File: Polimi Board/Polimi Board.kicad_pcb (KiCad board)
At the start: 2 copper layers, 96 parts, among them IC1 M95512-RMN6P, J1 I2C Oled Screen, J2 DM3AT-SF-PEJM5_40_, J3 65100516121, J4 UART Conn, J5 JTAG Conn, J7 65100516121, J8 7499010121A, SW1 MCU Reset, SW2 SW_Push, SW3 SW_Push, SW4 SW_Push, SW5 SW_Push, SW6 SW_Push, SW7 SW_Push, SW8 SW_Push, U1 STM32F205RCT6, U2 FT2232HL, U3 LAN8742A, U5 TLV76133DCY, Y1 ABL-25.000MHz-B1UB, Y2 ABL-12.000MHZ-20-D4HFI

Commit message: PCB wip
before holidays
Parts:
- removed R33, R34, R35, R36, R37, R38, R39: 47k, Resistor_SMD:R_0603_1608Metric_Pad0.98x0.95mm_HandSolder
- removed U5: TLV76133DCY, Package_TO_SOT_SMD:SOT-223-3_TabPin2
- added J6: DM3AT-SF-PEJM5_40_, SamacSys_Parts:DM3ATSFPEJM540, F.Cu at (185.7, 106.4)
- added J9: Conn_01x07_Pin, Connector_PinHeader_2.54mm:PinHeader_1x07_P2.54mm_Vertical, F.Cu at (197.8, 82.5)
- added R10: 47k, Resistor_SMD:R_0603_1608Metric_Pad0.98x0.95mm_HandSolder, F.Cu at (178.6, 107.9)
- added R11: 47k, Resistor_SMD:R_0603_1608Metric_Pad0.98x0.95mm_HandSolder, F.Cu at (181.3, 107.8)
- added R12: 47k, Resistor_SMD:R_0603_1608Metric_Pad0.98x0.95mm_HandSolder, F.Cu at (181.3, 111.5)
- added R14: 47k, Resistor_SMD:R_0603_1608Metric_Pad0.98x0.95mm_HandSolder, F.Cu at (178.6, 111.5)
- added R15: 47k, Resistor_SMD:R_0603_1608Metric_Pad0.98x0.95mm_HandSolder, F.Cu at (176.1, 111.5)
- added R9: 47k, Resistor_SMD:R_0603_1608Metric_Pad0.98x0.95mm_HandSolder, F.Cu at (176.1, 107.9)
- added REF**: MountingHole_3.2mm_M3_DIN965_Pad, MountingHole:MountingHole_3.2mm_M3_DIN965_Pad, F.Cu at (106.0, 45.0)
- added REF**: MountingHole_3.2mm_M3_DIN965_Pad, MountingHole:MountingHole_3.2mm_M3_DIN965_Pad, F.Cu at (198.0, 45.0)
- added REF**: MountingHole_3.2mm_M3_DIN965_Pad, MountingHole:MountingHole_3.2mm_M3_DIN965_Pad, F.Cu at (198.0, 137.0)
- added REF**: MountingHole_3.2mm_M3_DIN965_Pad, MountingHole:MountingHole_3.2mm_M3_DIN965_Pad, F.Cu at (106.0, 137.0)
- added U4: TLV76133DCY, Package_TO_SOT_SMD:SOT-223-3_TabPin2, F.Cu at (163.1, 56.6)
- J2: value DM3AT-SF-PEJM5_40_ -> 65100516121; footprint SamacSys_Parts:DM3ATSFPEJM540 -> SamacSys_Parts:65100516121
- J7: value 65100516121 -> 7499010121A; footprint SamacSys_Parts:65100516121 -> SamacSys_Parts:WURTH-7499010121A
- J8: value 7499010121A -> Conn_01x07_Pin; footprint SamacSys_Parts:WURTH-7499010121A -> Connector_PinHeader_2.54mm:PinHeader_1x07_P2.54mm_Vertical
- SW2: value SW_Push -> Boot
- moved R30 84.0 mm to (183.5, 130.2), turned to 180 degrees
- moved D1 83.4 mm to (172.2, 47.8), turned to 180 degrees
- moved R27 79.9 mm to (151.3, 134.1), turned to -90 degrees
- moved R29 79.5 mm to (172.0, 130.2), turned to 180 degrees
- moved R2 77.1 mm to (114.4, 62.9), turned to -90 degrees
- moved SW3 72.2 mm to (115.5, 122.0)
- moved R26 71.9 mm to (128.3, 126.0)
- moved R1 71.2 mm to (171.2, 53.5), turned to 90 degrees
- moved D4 71.0 mm to (157.2, 134.2), turned to 180 degrees
- moved R24 70.5 mm to (118.8, 118.5)
- moved JP4 66.6 mm to (109.5, 111.1), turned to -90 degrees
- moved SW8 66.4 mm to (180.4, 121.9)
- moved SW5 62.6 mm to (125.0, 129.4)
- moved SW7 61.0 mm to (168.7, 121.9)
- moved C23 59.4 mm to (116.3, 82.9), turned to 90 degrees
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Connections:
- J2 pad 1: /SDMMC_D2 -> /USB Programming and OTP/VBUS_PROG
- J2 pad 2: /SDMMC_D3 -> Net-(U2-DM)
- J2 pad 3: /SDMMC_CMD -> Net-(U2-DP)
- J2 pad 4: +3.3V -> unconnected-(J2-Pad4)
- J2 pad 5: /SDMMC_CK -> GND
- J3 pad 1: /USB Programming and OTP/VBUS_PROG -> /USB Programming and OTP/VBUS_OTG
- J3 pad 2: Net-(U2-DM) -> /OTG_DM
- J3 pad 3: Net-(U2-DP) -> /OTG_DP
- J7 pad 1: /USB Programming and OTP/VBUS_OTG -> /Ethernet/TXP
- J7 pad 2: /OTG_DM -> +3V3
- J7 pad 3: /OTG_DP -> /Ethernet/TXN
- J7 pad 4: unconnected-(J7-Pad4) -> /Ethernet/RXP
- J7 pad 5: GND -> +3V3
- J8 pad 1: /Ethernet/TXP -> +3.3V
- J8 pad 2: +3V3 -> /GPIO_EXT_1
- J8 pad 3: /Ethernet/TXN -> /GPIO_EXT_2
- J8 pad 4: /Ethernet/RXP -> /GPIO_EXT_3
- J8 pad 5: +3V3 -> /GPIO_EXT_4
- J8 pad 6: /Ethernet/RXN -> /GPIO_EXT_5
- J8 pad 7: unconnected-(J8-Pad7) -> GND
- R16 pad 1: Net-(J8-Pad11) -> Net-(J7-Pad10)
- R16 pad 2: GND -> /Ethernet/LED1
- R17 pad 1: Net-(J8-Pad9) -> /Ethernet/LED2
- R17 pad 2: GND -> Net-(J7-Pad12)
- U1 pad 14: unconnected-(U1-PA0-Pad14) -> /GPIO_EXT_1
- U1 pad 16: unconnected-(U1-PA2-Pad16) -> /GPIO_EXT_2
- U1 pad 17: unconnected-(U1-PA3-Pad17) -> /GPIO_EXT_3
- U1 pad 26: unconnected-(U1-PB0-Pad26) -> /GPIO_EXT_4
- U1 pad 27: unconnected-(U1-PB1-Pad27) -> /GPIO_EXT_5
- U1 pad 28: unconnected-(U1-PB2-Pad28) -> /GPIO_EXT_6
- U1 pad 29: unconnected-(U1-PB10-Pad29) -> /GPIO_EXT_9
- U1 pad 38: /SDMMC_WP -> /GPIO_EXT_10
- U1 pad 61: unconnected-(U1-PB8-Pad61) -> /GPIO_EXT_7
- U1 pad 62: unconnected-(U1-PB9-Pad62) -> /GPIO_EXT_8
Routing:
- net GND: track 0.00 -> 171.4 mm
- net +3.3V: track 0.00 -> 103.0 mm
- net /USB Programming and OTP/JTAG_SRST: track 0.00 -> 54.1 mm
- net /Ethernet/RXN: track 0.00 -> 52.4 mm
- net /JTAG_TD0: track 0.00 -> 46.1 mm
- net /SDMMC_CMD: track 0.00 -> 45.6 mm
- net Net-(U2-DP): track 0.00 -> 45.0 mm, vias 0 -> 2
- net Net-(U2-DM): track 0.00 -> 44.7 mm, vias 0 -> 2
- net /JTAG_TRST: track 0.00 -> 36.5 mm
- net /Ethernet/TXP: track 0.00 -> 34.0 mm
- net /JTAG_TMS: track 0.00 -> 33.5 mm
- net /JTAG_TDI: track 0.00 -> 31.6 mm
- net /Flash_MOSI: track 0.00 -> 31.4 mm, vias 0 -> 2
- net /Ethernet/RXP: track 0.00 -> 30.6 mm
- net Net-(U2-ACBUS4): track 0.00 -> 29.9 mm
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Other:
- board outline added: 100 x 100 mm

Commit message: almost finish
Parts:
- added G***: LOGO, graphics:Logo, B.Cu at (141.0, 98.6)
- J4: value UART Conn -> UART
- JP4: value MCU_RST -> MCU RST
- moved SW1 82.0 mm to (107.5, 133.1), turned to 180 degrees
- moved J6 81.3 mm to (105.8, 121.3), turned to -90 degrees
- moved SW2 79.6 mm to (170.6, 107.2)
- moved R11 72.3 mm to (110.2, 120.7), turned to -90 degrees
- moved R12 71.4 mm to (110.2, 117.1), turned to 90 degrees
- moved R2 70.6 mm to (161.9, 115.1)
- moved R10 66.9 mm to (112.9, 120.6), turned to -90 degrees
- moved R14 65.9 mm to (112.9, 117.1), turned to 90 degrees
- moved R9 62.0 mm to (115.4, 120.6), turned to -90 degrees
- moved R15 60.9 mm to (115.4, 117.1), turned to 90 degrees
- moved J2 44.8 mm to (109.2, 70.4)
- moved JP2 43.3 mm to (142.0, 70.0), turned to 0 degrees
- moved C8 39.4 mm to (132.0, 103.0), turned to 180 degrees
- moved C5 38.8 mm to (132.0, 101.0), turned to 180 degrees
- moved JP1 38.0 mm to (136.0, 70.0), turned to 0 degrees
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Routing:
- net GND: track 171.4 -> 675.1 mm, vias 0 -> 14
- net +3.3V: track 103.0 -> 521.0 mm, vias 0 -> 16
- net /USART_TX: track 0.00 -> 156.6 mm, vias 0 -> 2
- net /USART_RX: track 0.00 -> 153.5 mm, vias 0 -> 2
- net /MCU_RST: track 17.8 -> 122.3 mm, vias 0 -> 3
- net /GPIO_EXT_10: track 0.00 -> 71.7 mm, vias 0 -> 1
- net /MCO: track 6.96 -> 77.3 mm, vias 0 -> 2
- net /GPIO_EXT_9: track 0.00 -> 69.2 mm, vias 0 -> 1
- net /GPIO_EXT_5: track 0.00 -> 67.4 mm, vias 0 -> 1
- net /GPIO1: track 0.00 -> 62.7 mm, vias 0 -> 1
- net /GPIO_EXT_4: track 0.00 -> 61.7 mm, vias 0 -> 2
- net /GPIO_EXT_7: track 0.00 -> 59.6 mm, vias 0 -> 2
- net /GPIO_EXT_6: track 0.00 -> 59.1 mm, vias 0 -> 1
- net +3V3: track 27.0 -> 85.7 mm, vias 0 -> 2
- net Net-(U1-BOOT0): track 9.45 -> 67.1 mm, vias 0 -> 1
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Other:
- board size 100 x 100 mm -> 100 x 70 mm
- board text added: "FS"
- board text added: "HS"
- board text added: "OTG DM"
- board text added: "OTG DP"

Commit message: Final version
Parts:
- D2: value TXLED -> tx
- D3: value RXLED -> rx
- moved G*** 1.69 mm to (140.0, 100.0)
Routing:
- net Net-(U2-DP): track 28.8 -> 31.5 mm
- net Net-(U2-DM): track 25.5 -> 27.5 mm
- net /ETH_RMII_TXD0: track 60.1 -> 59.2 mm
- net /ETH_RMII_TX_EN: track 51.8 -> 52.3 mm
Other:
- board text added: "STM32F205RCT6 Board V1.0"

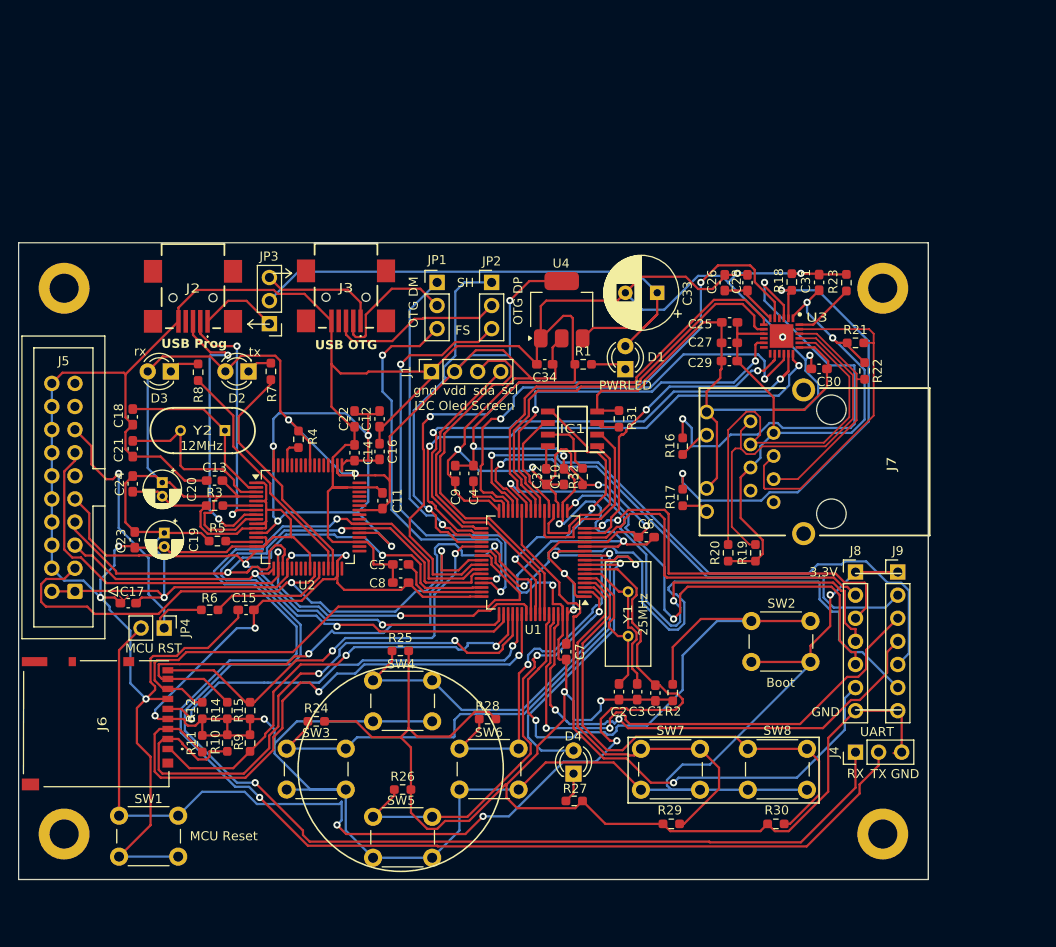
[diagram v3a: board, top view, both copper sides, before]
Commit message: Set zero at top left corner of PCB
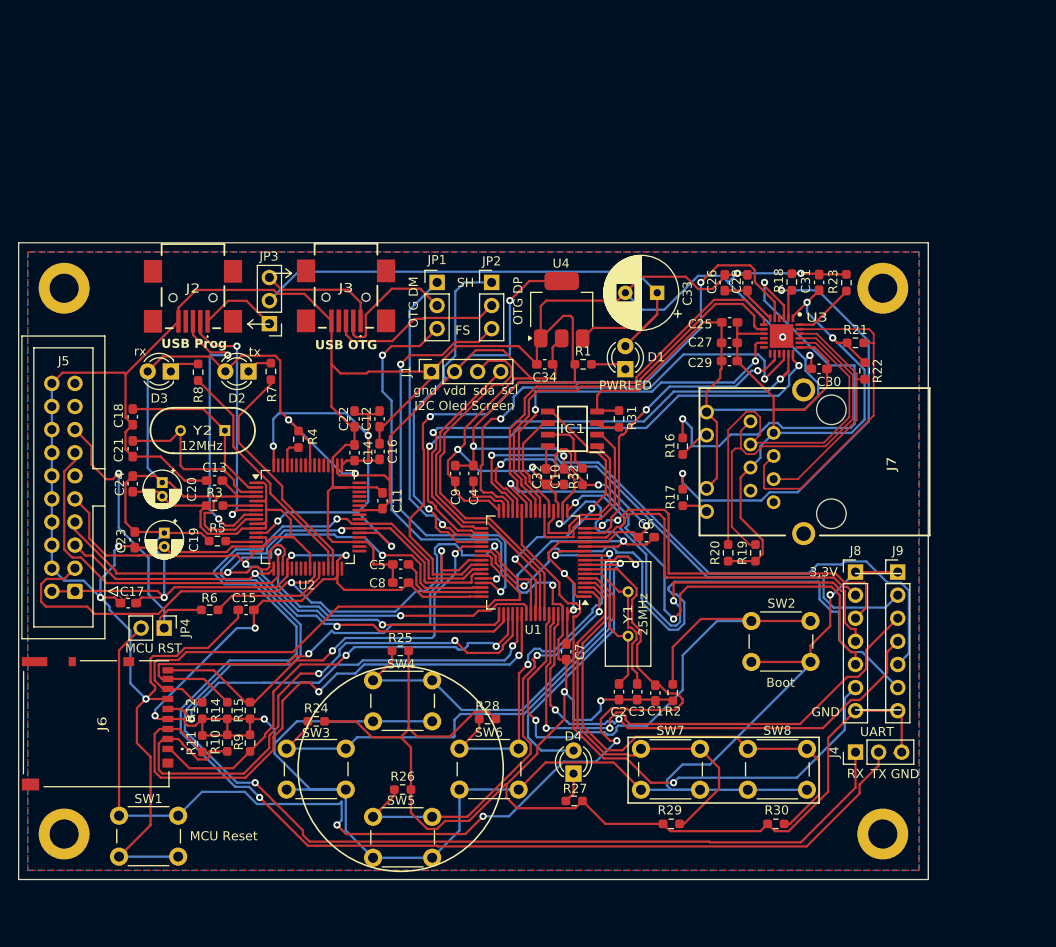
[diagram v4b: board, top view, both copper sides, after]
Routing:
- net +1V8: track 68.6 -> 60.1 mm
- added copper zone on B.Cu, net GND
- added copper zone on F.Cu, net GND
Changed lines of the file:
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@@
 		(pad_to_mask_clearance 0)
 		(allow_soldermask_bridges_in_footprints no)
+		(grid_origin 90 65.64)
 		(pcbplotparams
 			(layerselection 0x00010fc_ffffffff)
@@
 	)
 	(segment
-		(start 118 95.732888)
-		(end 118.495647 96.228535)
-		(width 0.25)
-		(layer "B.Cu")
-		(net 8)
-	)
-	(segment
 		(start 128.431375 86.824734)
 		(end 125.992063 84.385422)
@@
 	)
 	(segment
-		(start 118 88)
-		(end 118 95.732888)
-		(width 0.25)
-		(layer "B.Cu")
-		(net 8)
-	)
-	(segment
 		(start 128.431375 86.824734)
 		(end 128.431375 94.118625)
@@
 		(net 141)
 	)
+	(zone
+		(net 1)
+		(net_name "GND")
+		(layer "F.Cu")
+		(hatch edge 0.5)
+		(connect_pads
+			(clearance 0.5)
+		)
+		(min_thickness 0.25)
+		(filled_areas_thickness no)
+		(fill yes
+			(thermal_gap 0.5)
+			(thermal_bridge_width 0.5)
+		)
+		(polygon
+			(pts
+				(xy 91 66.64) (xy 189 66.64) (xy 189 134.64) (xy 91 134.64)
+			)
+		)
+	)
+	(zone
+		(net 1)
+		(net_name "GND")
+		(layer "B.Cu")
+		(hatch edge 0.5)
+		(priority 1)
+		(connect_pads
+			(clearance 0.5)
+		)
+		(min_thickness 0.25)
+		(filled_areas_thickness no)
+		(fill yes
+			(thermal_gap 0.5)
+			(thermal_bridge_width 0.5)
+		)
+		(polygon
+			(pts
+				(xy 189 66.64) (xy 91 66.64) (xy 91 134.64) (xy 189 134.64)
+			)
+		)
+	)
 	(group ""

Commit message: Solved issues
3.3V 3V3 and others
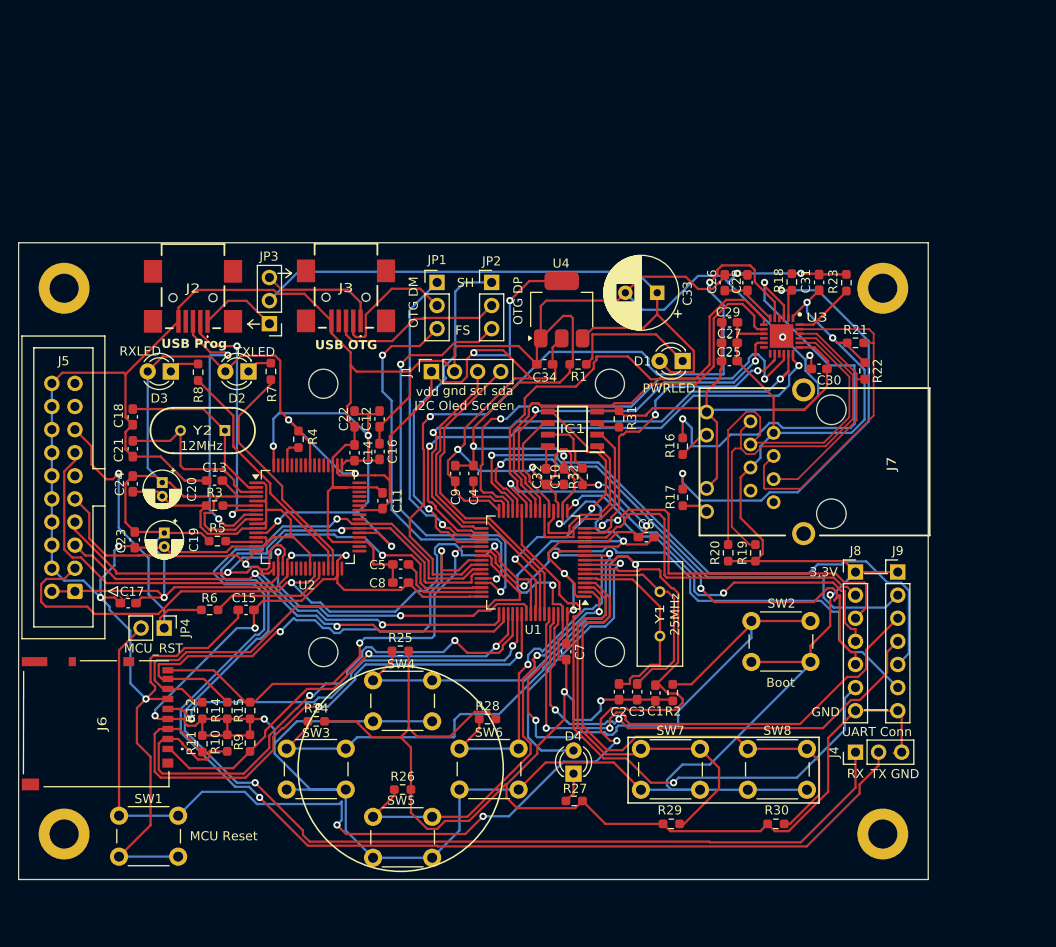
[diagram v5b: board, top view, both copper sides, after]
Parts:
- added G***: LOGO, graphics:oled, F.Cu at (140.8, 97.2)
- added REF**: MountingHole_3.2mm_M3_DIN965, MountingHole:MountingHole_3.2mm_M3_DIN965, F.Cu at (155.0, 81.1)
- added REF**: MountingHole_3.2mm_M3_DIN965, MountingHole:MountingHole_3.2mm_M3_DIN965, F.Cu at (123.5, 110.6)
- added REF**: MountingHole_3.2mm_M3_DIN965, MountingHole:MountingHole_3.2mm_M3_DIN965, F.Cu at (155.0, 110.6)
- added REF**: MountingHole_3.2mm_M3_DIN965, MountingHole:MountingHole_3.2mm_M3_DIN965, F.Cu at (123.5, 81.1)
- D2: value tx -> TXLED
- D3: value rx -> RXLED
- J4: value UART -> UART Conn
- JP4: value MCU RST -> MCU_RST
- moved D1 6.36 mm to (163.0, 78.6), turned to 180 degrees
- moved Y1 3.50 mm to (160.5, 104.0)
- moved G*** 1.00 mm to (139.0, 100.0)
- moved R1 0.56 mm to (151.5, 79.0)
- turned REF** to 0 degrees
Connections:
- C25 pad 1: +3V3 -> +3.3V
- C27 pad 1: +3V3 -> +3.3V
- C29 pad 1: +3V3 -> +3.3V
- C30 pad 1: +3V3 -> +3.3V
- C31 pad 1: +3V3 -> +3.3V
- J1 pad 1: GND -> +3.3V
- J1 pad 2: +3.3V -> GND
- J1 pad 3: /Oled_SDA_I2C -> /Oled_SCL_I2C
- J1 pad 4: /Oled_SCL_I2C -> /Oled_SDA_I2C
- J7 pad 2: +3V3 -> +3.3V
- J7 pad 5: +3V3 -> +3.3V
- R19 pad 1: +3V3 -> +3.3V
- R20 pad 1: +3V3 -> +3.3V
- R21 pad 1: +3V3 -> +3.3V
- R22 pad 1: +3V3 -> +3.3V
- U3 pad 1: +3V3 -> +3.3V
- U3 pad 19: +3V3 -> +3.3V
- U3 pad 9: +3V3 -> +3.3V
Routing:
- net +3.3V: track 521.0 -> 619.1 mm, vias 16 -> 19
- net +3V3: track 85.7 -> 0.00 mm, vias 2 -> 0
- net /GPIO_EXT_10: track 71.7 -> 59.7 mm
- net Net-(D1-K): track 3.95 -> 14.7 mm
- net /GPIO_EXT_3: track 53.6 -> 44.3 mm
- net GND: track 675.1 -> 665.9 mm
- net /MCO: track 77.3 -> 85.1 mm
- net USB_Vcc: track 61.5 -> 68.9 mm
- net /USART_RX: track 153.5 -> 146.9 mm
- net /USART_TX: track 156.6 -> 150.0 mm
- net Net-(U1-PH1): track 16.7 -> 22.9 mm
- net /Oled_SDA_I2C: track 41.8 -> 35.7 mm
- net Net-(U1-PH0): track 15.9 -> 21.6 mm
- net /ETH_RMII_RXD1: track 46.5 -> 52.1 mm
- net /GPIO_EXT_4: track 61.7 -> 57.1 mm
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- removed copper zone on B.Cu, net GND
- removed copper zone on F.Cu, net GND

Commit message: Solved filled zones
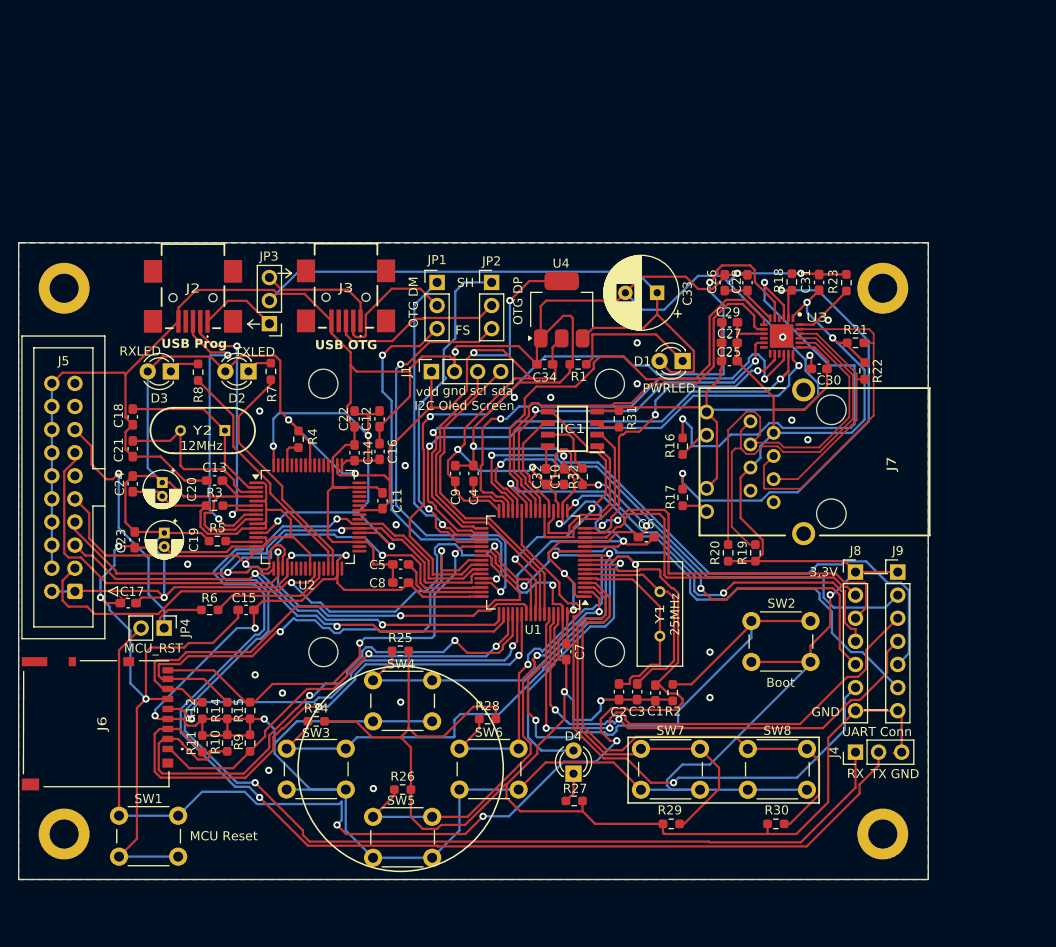
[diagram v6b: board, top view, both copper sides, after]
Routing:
- net /JTAG_TRST: track 79.7 -> 75.1 mm
- net GND: track 665.9 -> 663.3 mm, vias 14 -> 33
- net /GPIO_EXT_4: track 57.1 -> 55.2 mm
- net +3.3V: track 619.1 -> 620.7 mm
- net /GPIO_EXT_10: track 59.7 -> 60.6 mm
- net /MCO: track 85.1 -> 84.2 mm
- net /Ethernet/TXP: track 42.8 -> 43.3 mm
- added copper zone on B.Cu, net GND
- added copper zone on F.Cu, net GND
